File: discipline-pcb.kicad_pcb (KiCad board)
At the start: 2 copper layers, 304.9 x 122.8 mm, 197 parts, among them J1 AVR-ISP-6, SW1 KEYSW, SW10 KEYSW, SW11 KEYSW, SW12 KEYSW, SW13 KEYSW, SW14 KEYSW, SW15 KEYSW, SW16 KEYSW, SW17 KEYSW, SW18 KEYSW, SW19 KEYSW, SW2 KEYSW, SW20 KEYSW, SW21 KEYSW, SW22 KEYSW, SW23 KEYSW, SW24 KEYSW, SW25 KEYSW, SW26 KEYSW, SW27 KEYSW, SW28 KEYSW, SW29 KEYSW, SW3 KEYSW, SW30 KEYSW, SW31 KEYSW, SW32 KEYSW, SW33 KEYSW, SW34 KEYSW, SW35 KEYSW, SW36 KEYSW, SW37 KEYSW, SW38 KEYSW, SW39 KEYSW, SW4 KEYSW, SW40 KEYSW, SW41 KEYSW, SW42 KEYSW, SW43 KEYSW, SW44 KEYSW, SW45 KEYSW, SW46 KEYSW, SW47 KEYSW, SW48 KEYSW, SW49 KEYSW, SW5 KEYSW, SW50 KEYSW, SW51 KEYSW, SW52 KEYSW, SW53 KEYSW, SW54 KEYSW, SW55 KEYSW, SW56 KEYSW, SW57 KEYSW, SW58 KEYSW, SW59 KEYSW, SW6 KEYSW, SW60 KEYSW, SW61 KEYSW, SW62 KEYSW, SW63 KEYSW, SW64 KEYSW, SW65 KEYSW, SW66 KEYSW, SW67 KEYSW, SW68 KEYSW, SW69 KEYSW, SW7 KEYSW, SW70 KEYSW, SW71 KEYSW, SW72 KEYSW, SW73 KEYSW, SW74 KEYSW, SW75 KEYSW, SW76 KEYSW, SW77 KEYSW, SW78 KEYSW, SW8 KEYSW, SW9 KEYSW, U1 ATmega32A-PU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

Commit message: Replace keyswitch footprint with MX_Alps_Hybrid
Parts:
- SW1, SW10, SW11, SW12, SW13, SW15, SW17, SW18, SW19, SW2, SW20, SW21, SW22, SW23, SW24, SW25, SW26, SW27, SW28, SW3, SW30, SW32, SW33, SW34, SW35, SW36, SW37, SW38, SW39, SW4, SW40, SW41, SW42, SW44, SW46, SW47, SW48, SW49, SW5, SW50, SW51, SW52, SW53, SW54, SW55, SW57, SW58, SW6, SW62, SW65, SW66, SW67, SW68, SW7, SW72, SW75, SW77, SW8, SW9: footprint cftkb:SW_Cherry_MX1A_1.00u_PCB-NOSCREEN -> MX_Alps_Hybrid:MX-1U
- SW14: footprint cftkb:SW_Cherry_MX1A_2.00u_PCBNOSCREEN -> MX_Alps_Hybrid:MX-2U
- SW16, SW29, SW70, SW71, SW73, SW74: footprint cftkb:SW_Cherry_MX1A_1.50u_PCBNOSCREEN -> MX_Alps_Hybrid:MX-1.5U
- SW31, SW56: footprint cftkb:SW_Cherry_MX1A_1.75u_PCBNOSCREEN -> MX_Alps_Hybrid:MX-1.75U
- SW43, SW45: footprint cftkb:SW_Cherry_MX1A_2.25u_PCBNOSCREEN -> MX_Alps_Hybrid:MX-2.25U
- SW59, SW60, SW61, SW63, SW64, SW69, SW78: footprint cftkb:SW_Cherry_MX1A_1.25u_PCBNOSCREEN -> MX_Alps_Hybrid:MX-1.25U
- SW76: footprint cftkb:SW_Cherry_MX1A_ISOEnter_PCB_ReversedStabilizer -> cftkb:MX_Alps_Hybrid_ISOEnter_PCB_ReversedStabilizer
- moved SW10 5.68 mm to (234.8, 94.8)
- moved SW11 5.68 mm to (253.8, 94.8)
- moved SW15 5.68 mm to (349.1, 94.8)
- moved SW5 5.68 mm to (139.5, 94.8)
- moved SW50 5.68 mm to (182.4, 151.9)
- moved SW54 5.68 mm to (258.6, 151.9)
- moved SW55 5.68 mm to (277.7, 151.9)
- moved SW56 5.68 mm to (303.8, 151.9)
- moved SW57 5.68 mm to (330.0, 151.9)
- moved SW58 5.68 mm to (349.1, 151.9)
- moved SW2 5.68 mm to (82.4, 94.8)
- moved SW3 5.68 mm to (101.4, 94.8)
- moved SW4 5.68 mm to (120.5, 94.8)
- moved SW45 5.68 mm to (75.2, 151.9)
- moved SW46 5.68 mm to (106.2, 151.9)
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
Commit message: Remove ISO layout, add led matrix to schematic
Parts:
- removed the REF** at (184.8, 171.0)
- removed ST72: 7U, cftkb:MX-7U-Stabilizer
- removed SW69, SW78: KEYSW, MX_Alps_Hybrid:MX-1.25U
- removed SW70, SW71, SW73, SW74: KEYSW, MX_Alps_Hybrid:MX-1.5U
- removed SW72, SW75, SW77: KEYSW, MX_Alps_Hybrid:MX-1U
- removed SW76: KEYSW, cftkb:MX_Alps_Hybrid_ISOEnter_PCB_ReversedStabilizer
- SW62: footprint MX_Alps_Hybrid:MX-1U -> MX_Alps_Hybrid:MX-6.25U-ReversedStabilizers
- SW63, SW64: footprint MX_Alps_Hybrid:MX-1.25U -> MX_Alps_Hybrid:MX-1U
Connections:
- SW1 pad 3: (no net) -> CA2
- SW1 pad 4: (no net) -> CA1
- SW10 pad 3: (no net) -> CB3
- SW10 pad 4: (no net) -> CB1
- SW11 pad 3: (no net) -> CB4
- SW11 pad 4: (no net) -> CB1
- SW12 pad 3: (no net) -> CB5
- SW12 pad 4: (no net) -> CB1
- SW13 pad 3: (no net) -> CB6
- SW13 pad 4: (no net) -> CB1
- SW14 pad 3: (no net) -> CB7
- SW14 pad 4: (no net) -> CB1
- SW15 pad 3: (no net) -> CB8
- SW15 pad 4: (no net) -> CB1
- SW16 pad 3: (no net) -> CA1
- SW16 pad 4: (no net) -> CA2
- SW17 pad 3: (no net) -> CA3
- SW17 pad 4: (no net) -> CA2
- SW18 pad 3: (no net) -> CA4
- SW18 pad 4: (no net) -> CA2
- SW19 pad 3: (no net) -> CA5
- SW19 pad 4: (no net) -> CA2
- SW2 pad 3: (no net) -> CA3
- SW2 pad 4: (no net) -> CA1
- SW20 pad 3: (no net) -> CA6
- SW20 pad 4: (no net) -> CA2
- SW21 pad 3: (no net) -> CA7
- SW21 pad 4: (no net) -> CA2
- SW22 pad 3: (no net) -> CA8
- SW22 pad 4: (no net) -> CA2
- SW23 pad 3: (no net) -> CA9
- SW23 pad 4: (no net) -> CA2
- SW24 pad 3: (no net) -> CB1
- SW24 pad 4: (no net) -> CB2
- SW25 pad 3: (no net) -> CB3
- SW25 pad 4: (no net) -> CB2
- SW26 pad 3: (no net) -> CB4
- SW26 pad 4: (no net) -> CB2
- SW27 pad 3: (no net) -> CB5
- SW27 pad 4: (no net) -> CB2
- SW28 pad 3: (no net) -> CB6
- SW28 pad 4: (no net) -> CB2
- SW29 pad 3: (no net) -> CB7
- SW29 pad 4: (no net) -> CB2
- SW3 pad 3: (no net) -> CA4
- SW3 pad 4: (no net) -> CA1
- SW30 pad 3: (no net) -> CB8
- SW30 pad 4: (no net) -> CB2
- SW31 pad 3: (no net) -> CA1
- SW31 pad 4: (no net) -> CA3
- SW32 pad 3: (no net) -> CA2
- SW32 pad 4: (no net) -> CA3
- SW33 pad 3: (no net) -> CA4
- SW33 pad 4: (no net) -> CA3
- SW34 pad 3: (no net) -> CA5
- SW34 pad 4: (no net) -> CA3
- SW35 pad 3: (no net) -> CA6
- SW35 pad 4: (no net) -> CA3
- SW36 pad 3: (no net) -> CA7
- SW36 pad 4: (no net) -> CA3
- SW37 pad 3: (no net) -> CA8
- SW37 pad 4: (no net) -> CA3
- SW38 pad 3: (no net) -> Net-(SW38-Pad3)
- SW38 pad 4: (no net) -> CA3
- SW39 pad 3: (no net) -> CB1
- SW39 pad 4: (no net) -> CB3
- SW4 pad 3: (no net) -> CA5
- SW4 pad 4: (no net) -> CA1
- SW40 pad 3: (no net) -> CB2
- SW40 pad 4: (no net) -> CB3
- SW41 pad 3: (no net) -> CB4
- SW41 pad 4: (no net) -> CB3
- SW42 pad 3: (no net) -> CB5
- SW42 pad 4: (no net) -> CB3
- SW43 pad 3: (no net) -> CB7
- SW43 pad 4: (no net) -> CB3
- SW44 pad 3: (no net) -> CB8
- SW44 pad 4: (no net) -> CB3
- SW45 pad 3: (no net) -> CA1
- SW45 pad 4: (no net) -> CA4
- SW46 pad 3: (no net) -> CA3
- SW46 pad 4: (no net) -> CA4
- SW47 pad 3: (no net) -> CA5
- SW47 pad 4: (no net) -> CA4
- SW48 pad 3: (no net) -> CA6
- SW48 pad 4: (no net) -> CA4
- SW49 pad 3: (no net) -> CA7
- SW49 pad 4: (no net) -> CA4
- SW5 pad 3: (no net) -> CA6
- SW5 pad 4: (no net) -> CA1
- SW50 pad 3: (no net) -> CA8
- SW50 pad 4: (no net) -> CA4
- SW51 pad 3: (no net) -> CA9
- SW51 pad 4: (no net) -> CA4
- SW52 pad 3: (no net) -> CB1
- SW52 pad 4: (no net) -> CB4
- SW53 pad 3: (no net) -> CB2
- SW53 pad 4: (no net) -> CB4
- SW54 pad 3: (no net) -> CB3
- SW54 pad 4: (no net) -> CB4
- SW55 pad 3: (no net) -> CB5
- SW55 pad 4: (no net) -> CB4
- SW56 pad 3: (no net) -> CB6
- SW56 pad 4: (no net) -> CB4
- SW57 pad 3: (no net) -> CB7
- SW57 pad 4: (no net) -> CB4
- SW58 pad 3: (no net) -> CB8
- SW58 pad 4: (no net) -> CB4
- SW59 pad 3: (no net) -> CA1
- SW59 pad 4: (no net) -> CA5
- SW6 pad 3: (no net) -> CA7
- SW6 pad 4: (no net) -> CA1
- SW60 pad 3: (no net) -> CA2
- SW60 pad 4: (no net) -> CA5
- SW61 pad 3: (no net) -> CA3
- SW61 pad 4: (no net) -> CA5
- SW62 pad 3: (no net) -> CA8
- SW62 pad 4: (no net) -> CA5
- SW63 pad 3: (no net) -> CB2
- SW63 pad 4: (no net) -> CB5
- SW64 pad 3: (no net) -> CB3
- SW64 pad 4: (no net) -> CB5
- SW65 pad 3: (no net) -> CB6
- SW65 pad 4: (no net) -> CB5
- SW66 pad 3: (no net) -> CB7
- SW66 pad 4: (no net) -> CB5
- SW67 pad 3: (no net) -> CB8
- SW67 pad 4: (no net) -> CB5
- SW68 pad 3: (no net) -> CB4
- SW68 pad 4: (no net) -> CB5
- SW7 pad 3: (no net) -> CA8
- SW7 pad 4: (no net) -> CA1
- SW8 pad 3: (no net) -> CA9
- SW8 pad 4: (no net) -> CA1
- SW9 pad 3: (no net) -> CB2
- SW9 pad 4: (no net) -> CB1
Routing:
- net (no net): track 0.00 -> 2.99 mm, vias 0 -> 4
- net GND: track 223.5 -> 220.5 mm, vias 48 -> 44

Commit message: Misc cleanup, delete tracks to prepare for bigger changes
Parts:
- removed G*** (x2): LOGO, logos:rev1-1_16mm_copper
- removed G*** (x2): LOGO, logos:coseyfannitutti_16mm
- removed G***: LOGO, logos:TOPY 4MM MASK
- removed G*** (x2): LOGO, logos:DISCIPLINE_SMALL_MASK
- removed G*** (x2): LOGO, logos:DISCIPLINE_SMALL_COPPER
- removed G*** (x2): LOGO, logos:rev1-1_16mm_mask
- removed G*** (x2): LOGO, logos:coseyfannitutti_rev1_16mm_copper
- added TOPY2: MountingHole, cftkb:TOPY 4MM MASK, F.Cu at (354.1, 71.1)
- H1, H10, H11, H12, H2, H3, H4, H5, H6, H7, H8, H9: renamed from REF**; value MountingHole_2.2mm_M2_Pad -> MountingHole
- TOPY1: renamed from G***; value LOGO -> MountingHole; footprint logos:TOPY 4MM MASK -> cftkb:TOPY 4MM MASK
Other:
- board text removed: "1.25U"
- board text removed: "1.25U ISO"
- board text removed: "1.5U"
- board text removed: "1U"
- board text removed: "1U ISO"
- board text removed: "2.25U ANSI"
- board text removed: "ANSI ENTER"
- board text removed: "ISO ENTER"
- board text removed: "STANDARD"
- board text removed: "STEPPED"

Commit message: Move diodes to key area
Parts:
- removed D71: , cftkb:D_DO-35_SOD27_P5.08mm_Horizontal
- D1, D10, D11, D12, D13, D14, D15, D16, D17, D18, D19, D2, D20, D21, D22, D23, D24, D25, D26, D27, D28, D29, D3, D30, D31, D32, D33, D34, D35, D36, D37, D38, D39, D4, D40, D41, D42, D43, D44, D45, D46, D47, D48, D49, D5, D50, D51, D52, D53, D54, D55, D56, D57, D58, D59, D6, D60, D61, D62, D63, D64, D65, D66, D67, D68, D7, D8, D9: footprint cftkb:D_DO-35_SOD27_P5.08mm_Horizontal -> keyboard_parts:D_SOD123_axial; moved to B.Cu
- D69, D70: footprint cftkb:D_DO-35_SOD27_P5.08mm_Horizontal -> keyboard_parts:D_SOD123_axial
- moved D59 210.6 mm to (75.2, 171.0), turned to 90 degrees
- moved D61 168.9 mm to (122.9, 171.0), turned to 90 degrees
- moved D66 143.9 mm to (339.6, 171.0), turned to 90 degrees
- moved D67 137.2 mm to (357.1, 171.0), turned to 90 degrees
- moved D57 129.9 mm to (339.6, 151.9), turned to 90 degrees
- moved D65 128.3 mm to (320.5, 171.0), turned to 90 degrees
- moved D58 125.0 mm to (357.1, 151.9), turned to 90 degrees
- moved D56 123.0 mm to (313.4, 151.9), turned to 90 degrees
- moved D62 120.3 mm to (194.3, 171.0), turned to 90 degrees
- moved D68 115.1 mm to (301.5, 171.0), turned to 90 degrees
- moved D64 115.1 mm to (282.5, 171.0), turned to 90 degrees
- moved D29 113.1 mm to (334.8, 113.8), turned to 90 degrees
- moved D43 112.5 mm to (327.7, 132.9), turned to 90 degrees
- moved D55 110.0 mm to (287.2, 151.9), turned to 90 degrees
- moved D44 109.2 mm to (357.1, 132.9), turned to 90 degrees
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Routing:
- net Net-(D59-Pad2): track 462.2 -> 0.00 mm
- net Net-(D61-Pad2): track 425.1 -> 0.00 mm
- net row3: track 404.8 -> 0.00 mm, vias 7 -> 0
- net col0: track 364.4 -> 0.00 mm, vias 2 -> 0
- net Net-(D62-Pad2): track 355.8 -> 0.00 mm
- net col2: track 331.4 -> 0.00 mm, vias 2 -> 0
- net col1: track 317.4 -> 0.00 mm
- net row4: track 299.4 -> 0.00 mm
- net Net-(D63-Pad2): track 279.4 -> 0.00 mm
- net col6: track 277.6 -> 0.00 mm
- net row1: track 272.6 -> 0.00 mm, vias 4 -> 0
- net col5: track 269.8 -> 0.00 mm
- net col7: track 268.1 -> 0.00 mm
- net row0: track 267.2 -> 0.00 mm, vias 1 -> 0
- net col3: track 262.1 -> 0.00 mm
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
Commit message: Add power, oled, ble modules
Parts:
- added A1: BLUEFRUIT_SPI_FRIEND, Gigahawk:BLUEFRUIT_SPI_FRIEND, F.Cu at (68.1, 71.6)
- added A2: SSD1306_I2C_MODULE, Gigahawk:SSD1306_MODULE_128x32, F.Cu at (345.6, 62.7)

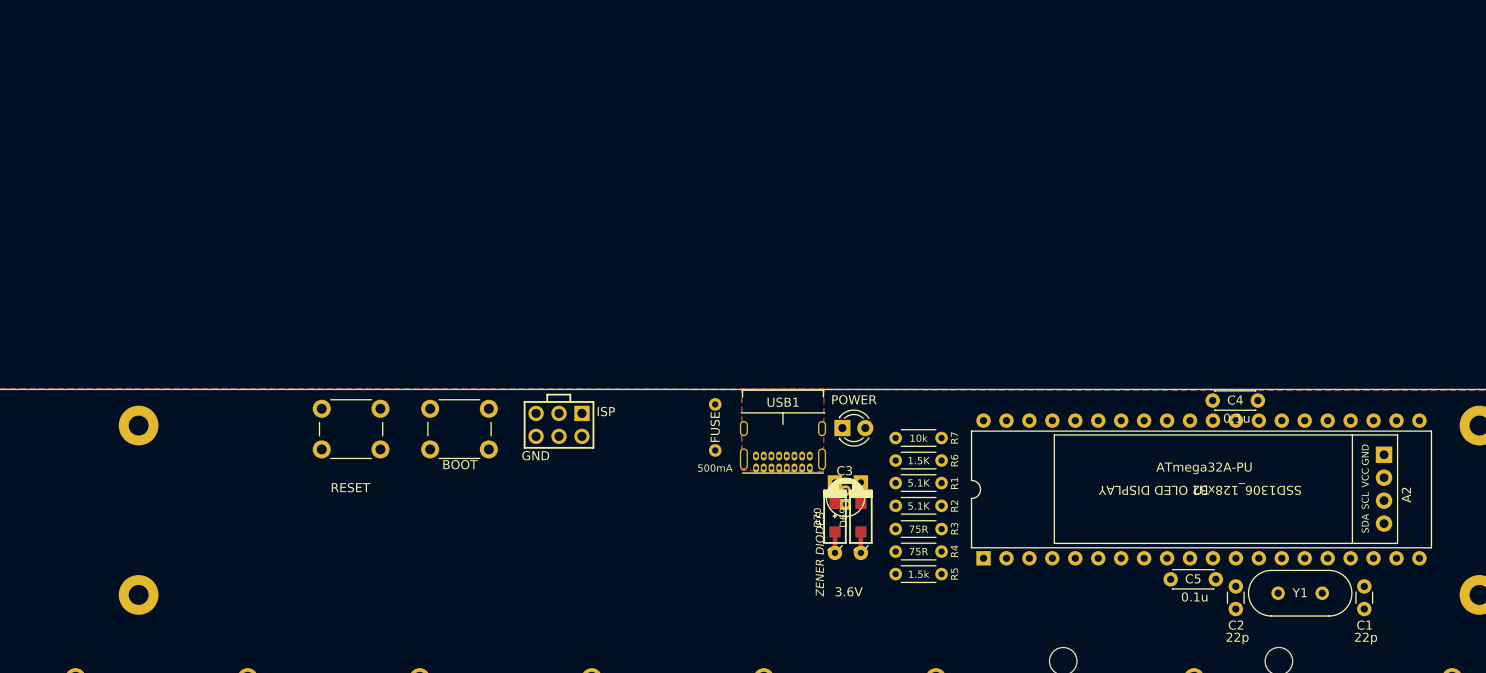
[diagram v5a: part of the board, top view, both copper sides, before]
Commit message: Add rotary encoder
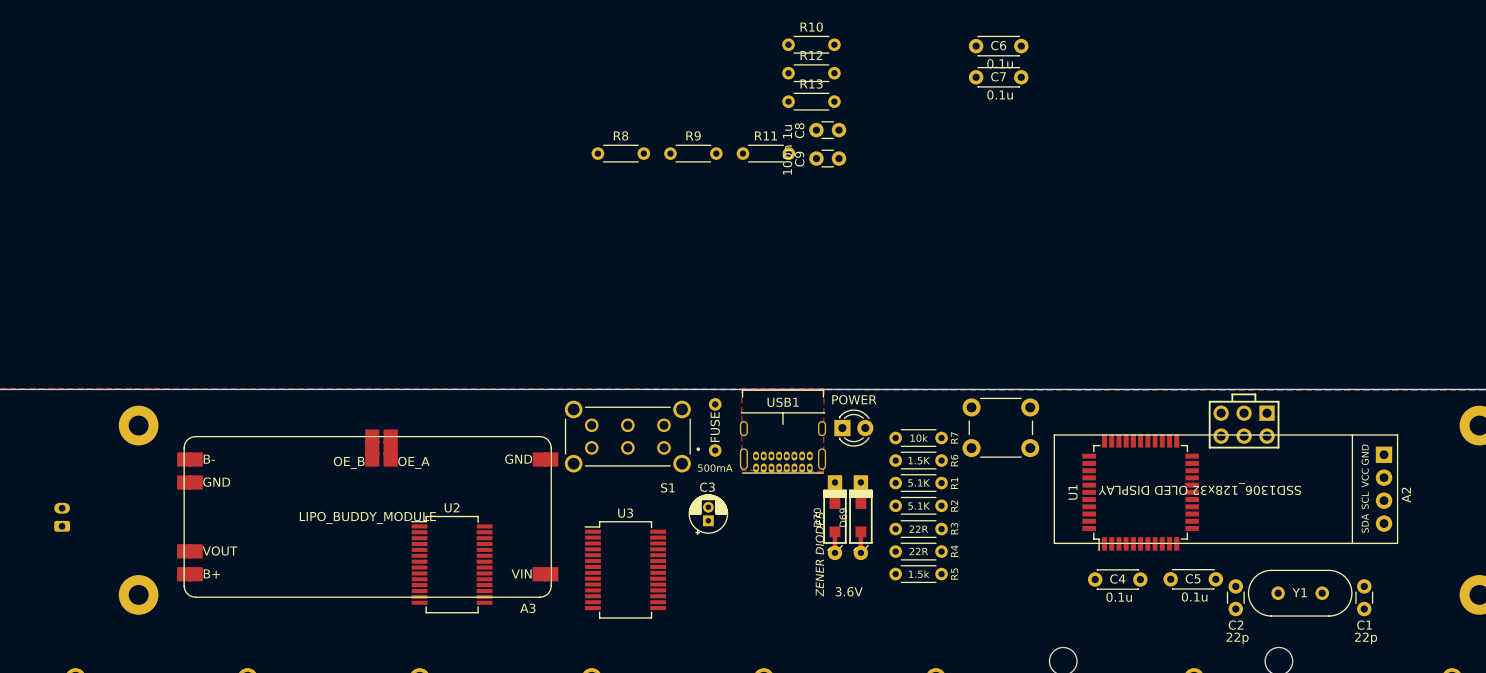
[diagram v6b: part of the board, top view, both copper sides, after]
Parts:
- removed BOOT1: BOOT, cftkb:SW_PUSH_6mm
- added A3: LIPO_BUDDY_MODULE, Gigahawk:LIPO_BUDDY_MODULE, F.Cu at (251.9, 80.7)
- added C6: 0.1u, cftkb:C_Disc_D4.3mm_W1.9mm_P5.00mm, F.Cu at (298.9, 19.7)
- added C7: 0.1u, cftkb:C_Disc_D4.3mm_W1.9mm_P5.00mm, F.Cu at (298.9, 23.1)
- added C8: 1u, cftkb:C_Disc_D3.0mm_W1.6mm_P2.50mm, F.Cu at (281.3, 29.0)
- added C9: 100n, cftkb:C_Disc_D3.0mm_W1.6mm_P2.50mm, F.Cu at (281.3, 32.1)
- added J2: Conn_01x02_Male, Connector_JST:JST_PH_S2B-PH-K_1x02_P2.00mm_Horizontal, B.Cu at (197.7, 72.8)
- added R10: 4.7k, cftkb:R_Axial_DIN0204_L3.6mm_D1.6mm_P5.08mm_Horizontal, F.Cu at (278.2, 19.5)
- added R11: 10k, cftkb:R_Axial_DIN0204_L3.6mm_D1.6mm_P5.08mm_Horizontal, F.Cu at (273.1, 31.6)
- added R12: 10k, cftkb:R_Axial_DIN0204_L3.6mm_D1.6mm_P5.08mm_Horizontal, F.Cu at (278.2, 22.7)
- added R13: 10k, cftkb:R_Axial_DIN0204_L3.6mm_D1.6mm_P5.08mm_Horizontal, F.Cu at (278.2, 25.8)
- added R8: 10k, cftkb:R_Axial_DIN0204_L3.6mm_D1.6mm_P5.08mm_Horizontal, F.Cu at (257.1, 31.6)
- added R9: 4.7k, cftkb:R_Axial_DIN0204_L3.6mm_D1.6mm_P5.08mm_Horizontal, F.Cu at (265.1, 31.6)
- added S1: EG2219, Gigahawk:SW_EG2219, F.Cu at (260.4, 62.9)
- added U2: MCP23017_SS, Package_SO:SSOP-28_5.3x10.2mm_P0.65mm, F.Cu at (240.9, 77.1)
- added U3: IS31FL3731-SA, Package_SO:SSOP-28_5.3x10.2mm_P0.65mm, F.Cu at (260.1, 77.7)
- R3, R4: value 75R -> 22R
- U1: value ATmega32A-PU -> ATMEGA32U4; footprint cftkb:DIP-40_W15.24mm -> Package_QFP:TQFP-44_10x10mm_P0.8mm
- Y1: value Crystal -> 16MHz
- moved J1 75.8 mm to (328.6, 61.6)
- moved RESET1 71.9 mm to (298.4, 59.7)
- moved C4 23.7 mm to (312.1, 78.7)
- moved U1 18.9 mm to (317.1, 69.1)
- moved C3 15.3 mm to (269.3, 72.2)
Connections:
- net Net-(A1-Pad6) renamed BLE_DFU
- A1 pad 1: Net-(A1-Pad1) -> SCK
- A1 pad 2: Net-(A1-Pad2) -> MISO
- A1 pad 3: Net-(A1-Pad3) -> MOSI
- A1 pad 4: Net-(A1-Pad4) -> BLE_CS
- A1 pad 5: Net-(A1-Pad5) -> BLE_IRQ
- A1 pad 7: Net-(A1-Pad7) -> BLE_RST
- A1 pad 8: Net-(A1-Pad8) -> GND
- A1 pad 9: Net-(A1-Pad9) -> +5V
- A2 pad 1: Net-(A2-Pad1) -> GND
- A2 pad 2: Net-(A2-Pad2) -> +5V
- A2 pad 3: Net-(A2-Pad3) -> SCL
- A2 pad 4: Net-(A2-Pad4) -> SDA
- F1 pad 1: +5V -> Net-(F1-Pad1)
- F1 pad 2: VCC -> VUSB
- R7 pad 2: reset -> MCU_RST
- RESET1 pad 1: reset -> MCU_RST
- U1 pad 1: row4 -> BLE_IRQ
- U1 pad 10: +5V -> MOSI
- U1 pad 11: GND -> MISO
- U1 pad 12: Net-(C2-Pad1) -> Net-(U1-Pad12)
- U1 pad 13: Net-(C1-Pad1) -> MCU_RST
- U1 pad 14: Net-(U1-Pad14) -> +5V
- U1 pad 15: Net-(U1-Pad15) -> GND
- U1 pad 16: D+ -> Net-(C1-Pad1)
- U1 pad 17: D- -> Net-(C2-Pad1)
- U1 pad 18: boot -> SCL
- U1 pad 19: col5 -> SDA
- U1 pad 2: row2 -> +5V
- U1 pad 20: col6 -> Net-(U1-Pad20)
- U1 pad 21: col14 -> Net-(U1-Pad21)
- U1 pad 22: col13 -> Net-(U1-Pad22)
- U1 pad 23: col12 -> GND
- U1 pad 24: col11 -> +5V
- U1 pad 25: col10 -> BLE_RST
- U1 pad 26: col9 -> Net-(U1-Pad26)
- U1 pad 27: col8 -> Net-(U1-Pad27)
- U1 pad 28: col7 -> BLE_CS
- U1 pad 3: row0 -> D-
- U1 pad 30: +5V -> Net-(U1-Pad30)
- U1 pad 31: GND -> Net-(U1-Pad31)
- U1 pad 34: Net-(U1-Pad34) -> +5V
- U1 pad 35: Net-(U1-Pad35) -> GND
- U1 pad 36: col4 -> Net-(U1-Pad36)
- U1 pad 37: col2 -> Net-(U1-Pad37)
- U1 pad 38: col0 -> Net-(U1-Pad38)
- U1 pad 39: row1 -> Net-(U1-Pad39)
- U1 pad 4: col1 -> D+
- U1 pad 40: row3 -> Net-(U1-Pad40)
- U1 pad 5: col3 -> GND
- U1 pad 6: MOSI -> Net-(C8-Pad2)
- U1 pad 7: MISO -> +5V
- U1 pad 8: SCK -> Net-(U1-Pad8)
- U1 pad 9: reset -> SCK
- USB1 pad A4: VCC -> Net-(F1-Pad1)
- USB1 pad A9: VCC -> Net-(F1-Pad1)
- USB1 pad B4: VCC -> Net-(F1-Pad1)
- USB1 pad B9: VCC -> Net-(F1-Pad1)
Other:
- board text removed: "GND"
- board text removed: "ISP"
- board text removed: "RESET"
